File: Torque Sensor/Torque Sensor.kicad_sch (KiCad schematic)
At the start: 23 parts, among them J2 Full Bridge Strain Guage, U3 AD7173-8

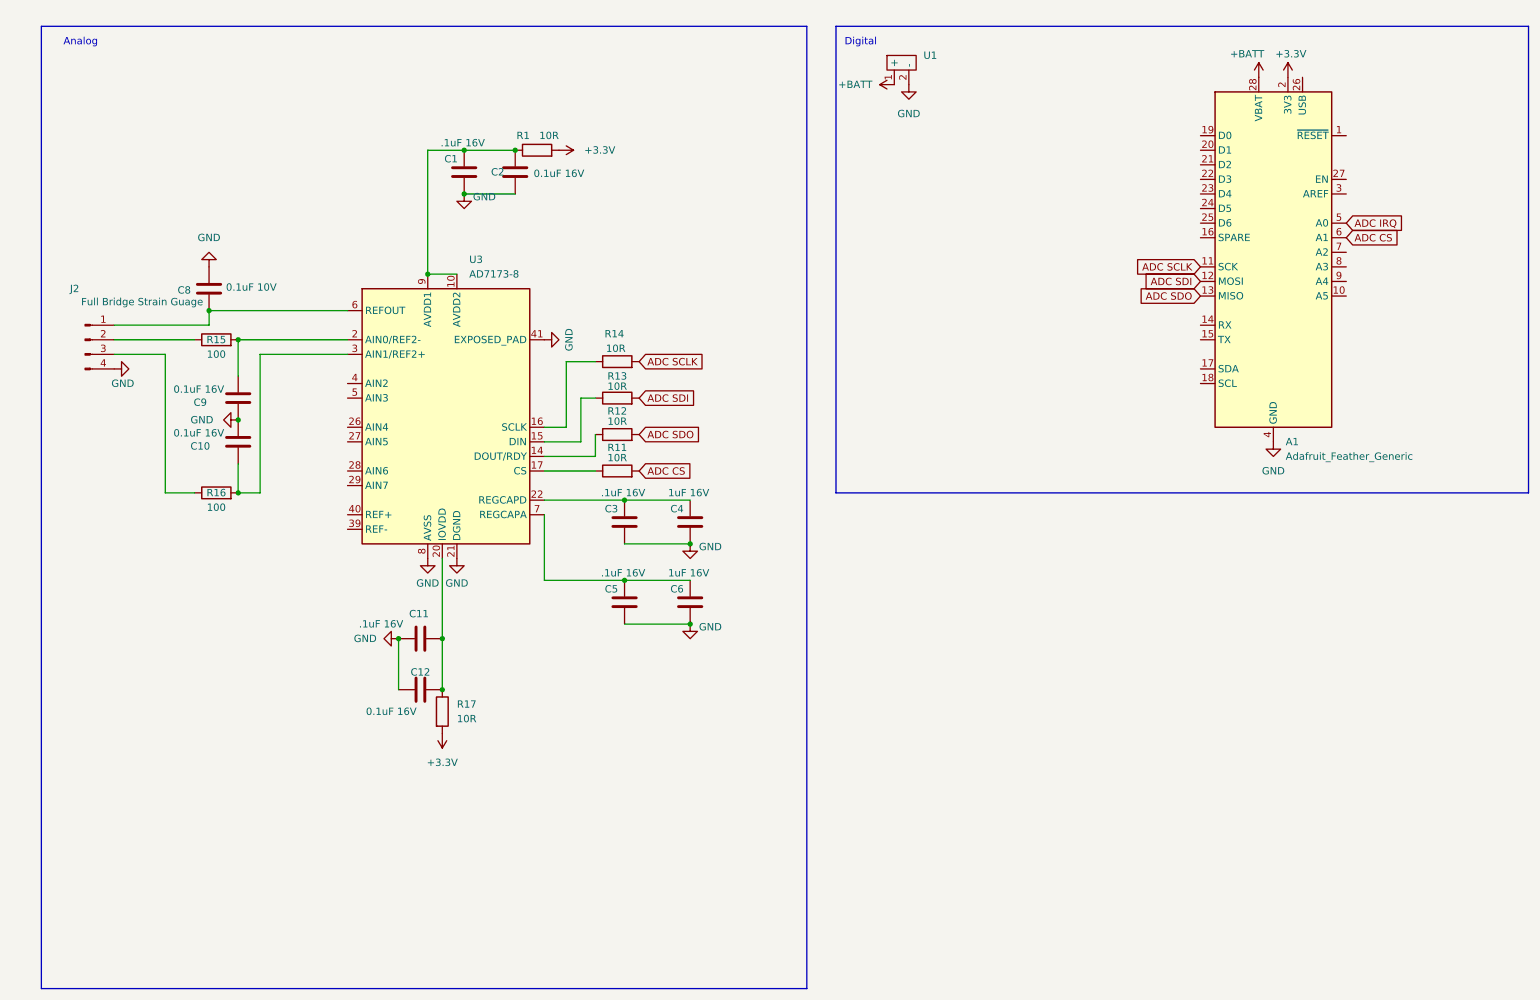
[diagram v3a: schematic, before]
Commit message: Rolled back to using QTPY with new charging circuitry
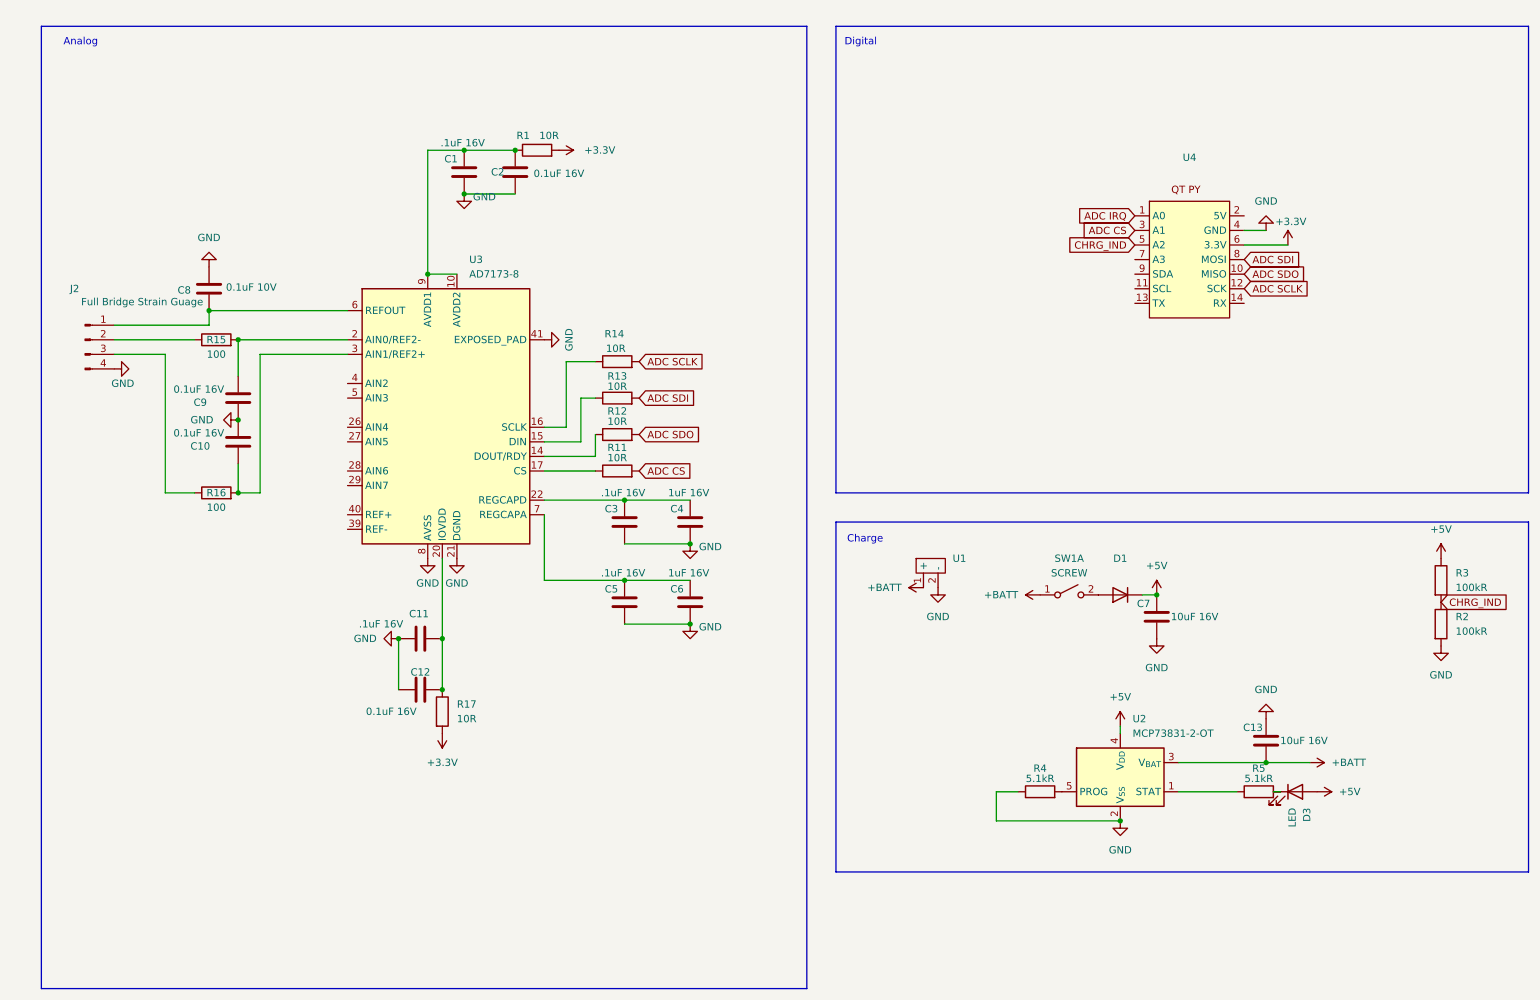
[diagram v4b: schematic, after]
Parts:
- removed A1: Adafruit_Feather_Generic, Module:Adafruit_Feather, symbol MCU_Module:Adafruit_Feather_Generic
- added C13, C7: 10uF 16V, Capacitor_SMD:C_0805_2012Metric, symbol Device:C
- added D1: ~, Diode_THT:D_DO-35_SOD27_P7.62mm_Horizontal, symbol Diode:1N914
- added D3: LED, symbol Device:LED
- added R2, R3: 100kR, Resistor_SMD:R_0805_2012Metric, symbol Device:R
- added R4, R5: 5.1kR, Resistor_SMD:R_0805_2012Metric, symbol Device:R
- added SW1: SCREW, symbol Switch:SW_DPST_x2
- added U2: MCP73831-2-OT, Package_TO_SOT_SMD:SOT-23-5, symbol Battery_Management:MCP73831-2-OT
- added U4: ~, TestLib:Adafruit QT PY, symbol New_Library:QT_PY
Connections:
- net +3.3V: now also U4.6 (3.3V)
- net +BATT: now also C13.1, SW1.1 (A), U2.3 (V_{BAT})
- net ADC CS: now also U4.3 (A1)
- net ADC IRQ: now also U4.1 (A0)
- net ADC SCLK: now also U4.12 (SCK)
- net ADC SDI: now also U4.8 (MOSI)
- net ADC SDO: now also U4.10 (MISO)
- net GND: now also C13.2, C7.1, R2.2, R4.1, U2.2 (V_{SS}), U4.4 (GND)
- new net: D1.2 (A), SW1.2 (B)
- new net: R4.2, U2.5 (PROG)
- new net: D3.1 (K), R5.2
- new net: R5.1, U2.1 (STAT)
- new net +5V: C7.2, D1.1 (K), D3.2 (A), R3.1, U2.4 (V_{DD})
- new net CHRG_IND: R2.1, R3.2, U4.5 (A2)
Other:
- note added: "Charge"
- moved on the sheet: U1

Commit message: Better style - connections explicitly shown.
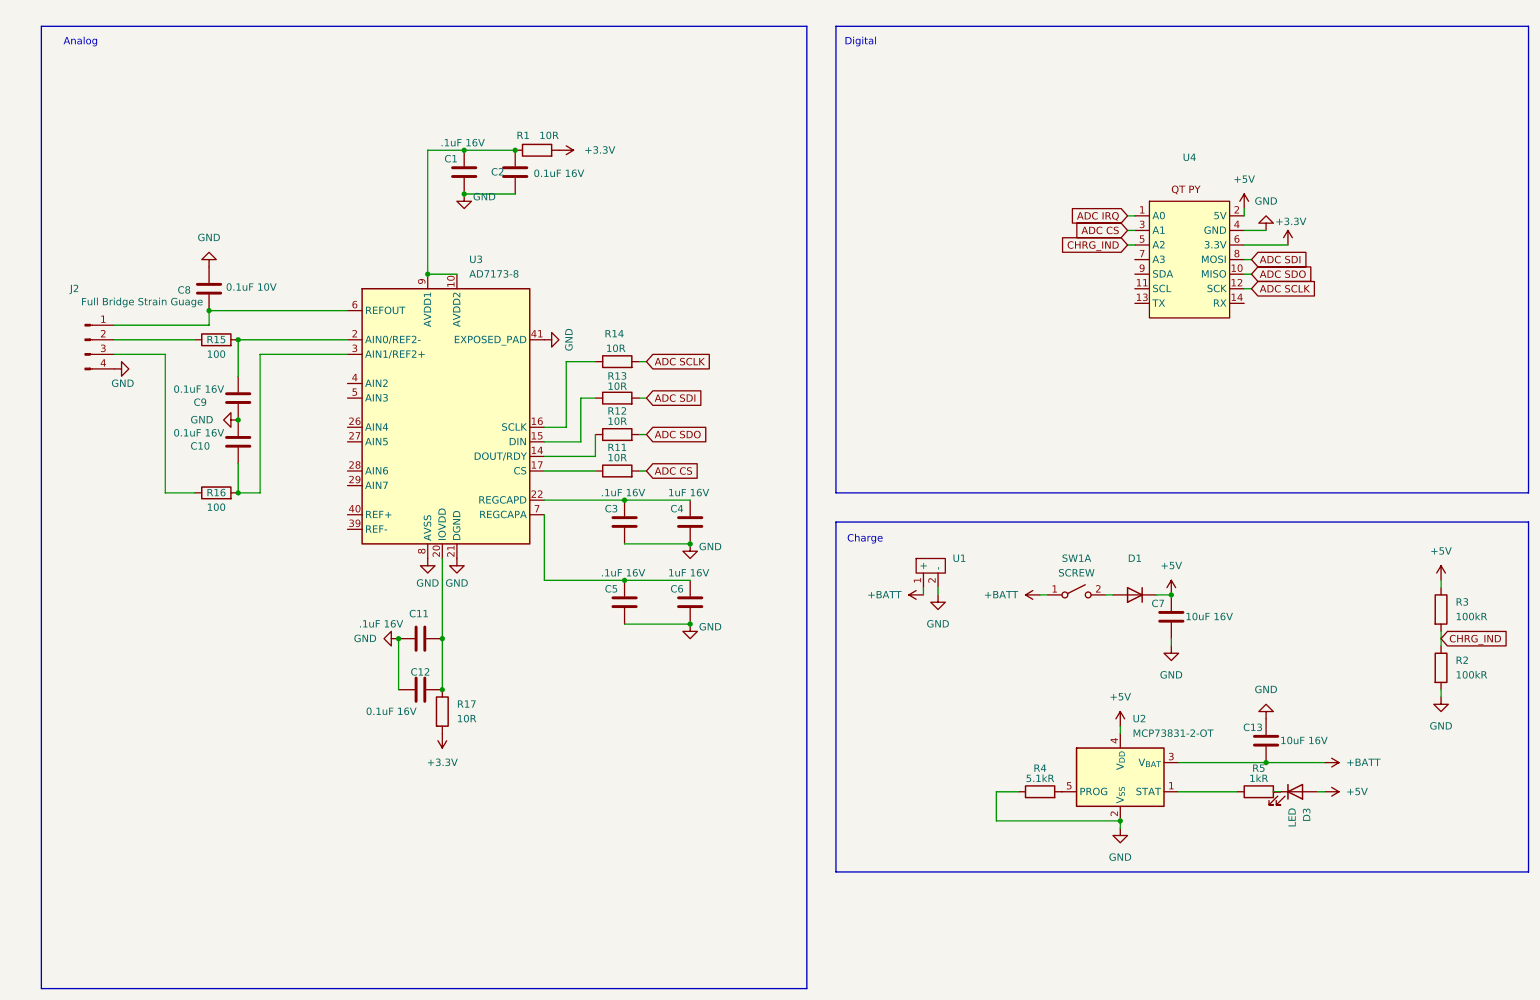
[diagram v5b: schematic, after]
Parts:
- D3: footprint (none) -> LED_SMD:LED_0805_2012Metric
- R5: value 5.1kR -> 1kR
- SW1: footprint (none) -> Connector_PinHeader_1.00mm:PinHeader_1x02_P1.00mm_Vertical
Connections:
- net +5V: now also U4.2 (5V)
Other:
- moved on the sheet: C7, D1, R2, R3, SW1A

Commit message: flipped QTPY to back
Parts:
- D1: footprint Diode_THT:D_DO-35_SOD27_P7.62mm_Horizontal -> Diode_SMD:D_SOD-323
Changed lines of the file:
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@@
 			)
 		)
-		(property "Footprint" "Diode_THT:D_DO-35_SOD27_P7.62mm_Horizontal"
+		(property "Footprint" "Diode_SMD:D_SOD-323"
 			(at 207.01 109.855 0)
 			(effects
